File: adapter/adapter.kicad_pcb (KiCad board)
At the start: 2 copper layers, 93.5 x 50.8 mm, 42 parts, among them J1 Serial, J10 Ribbon, J11 Ribbon, J12 Ribbon, J2 Serial, J3 battery charge, J4 RGB, J5 RGB, J6 battery charge, J7 trackball, J8 trackball, J9 Ribbon, SW1 SW_SPST, SW2 SW_SPST, SW3 SW_SPDT, SW4 SW_SPDT, U1 eliteC, U2 eliteC

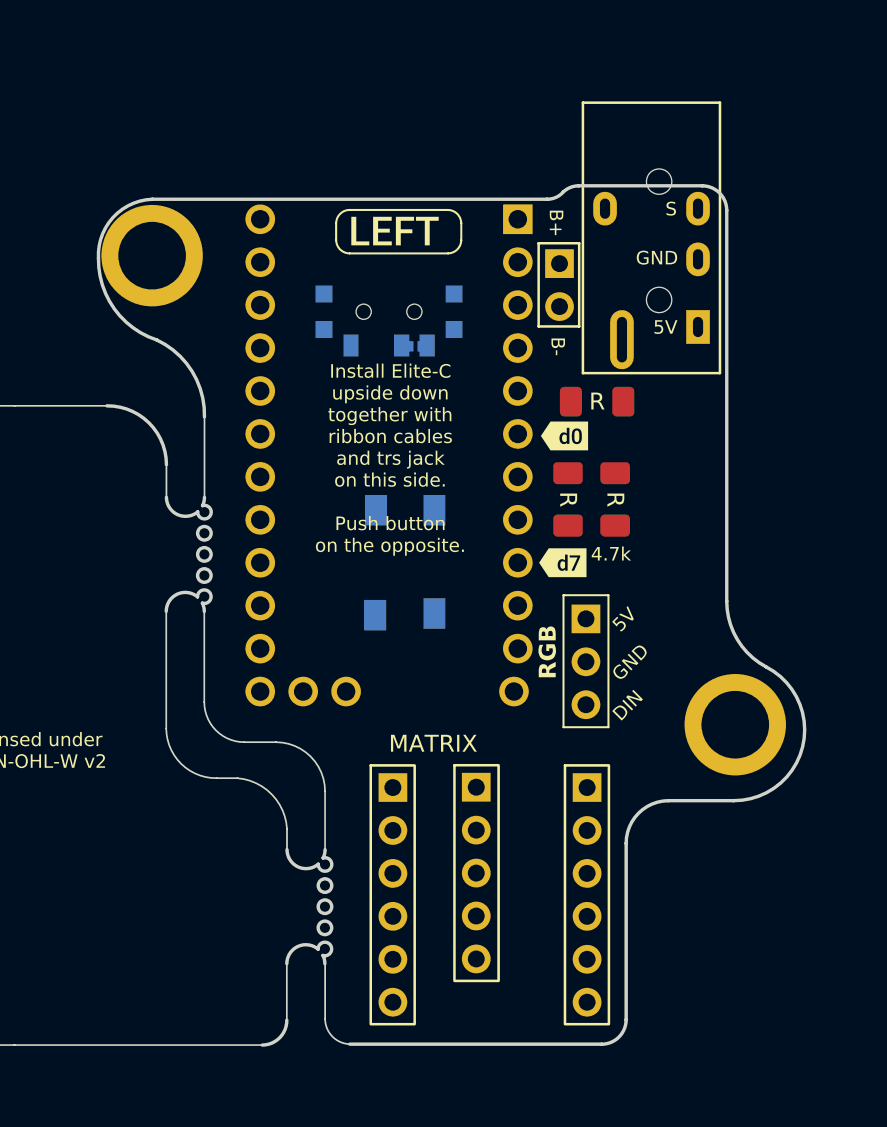
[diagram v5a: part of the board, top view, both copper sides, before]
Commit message: pcb: remove all footprints for rhs
Signed-off-by: Anant Thazhemadam <anant.thazhemadam@gmail.com>
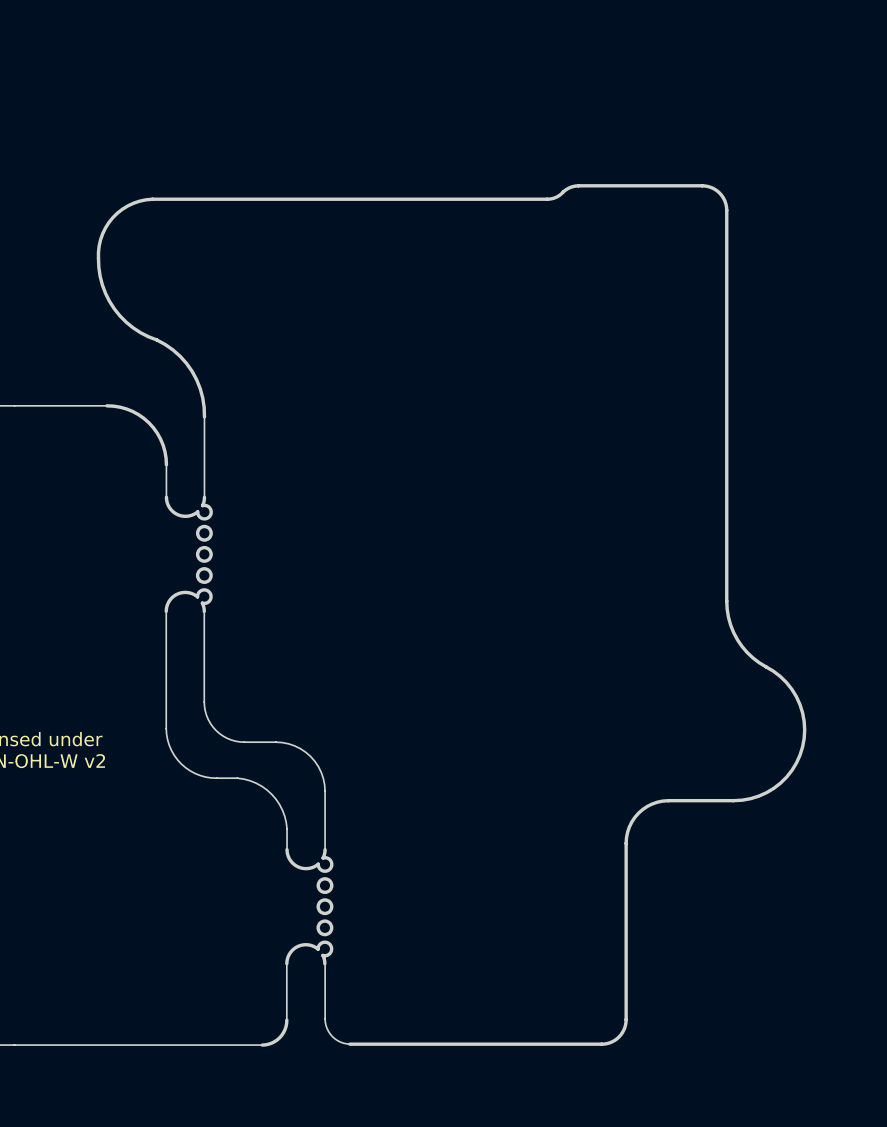
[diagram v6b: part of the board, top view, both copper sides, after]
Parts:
- removed H1, H3: M4, library:MountingHole_4mm_Pad_thin
- removed J11: Ribbon, library:5_PinHeader
- removed J12: Ribbon, library:6_PinHeader
- removed J2: Serial, library:Jack_3.5mm_PJ320E_Horizontal
- removed J5: RGB, library:header1x03
- removed J6: battery charge, library:PinHeader_1x02_P2.54mm_Vertical
- removed J8: trackball, library:6_PinHeader
- removed JP2: Jumper_2_Open, library:power_switch_jumper
- removed R1, R3, R5: 5.1k, library:R_1206_handsolder
- removed SW2: SW_SPST, library:PushSwitch
- removed SW4: SW_SPDT, library:SW_SPDT+H-MSK12C01_hor(7pin_SMD)
- removed U2: eliteC, library:Elite-C
- removed the kibuzzard-61F01C84 at (174.5, 89.2)
- removed kibuzzard-6208EE22: G***, kibuzzard-6208EE22
- removed kibuzzard-6208EFFE (x2): G***, kibuzzard-6208EFFE
- removed kibuzzard-62094D1C: G***, kibuzzard-62094D1C
- removed the kibuzzard-620B8593 at (177.5, 78.6)

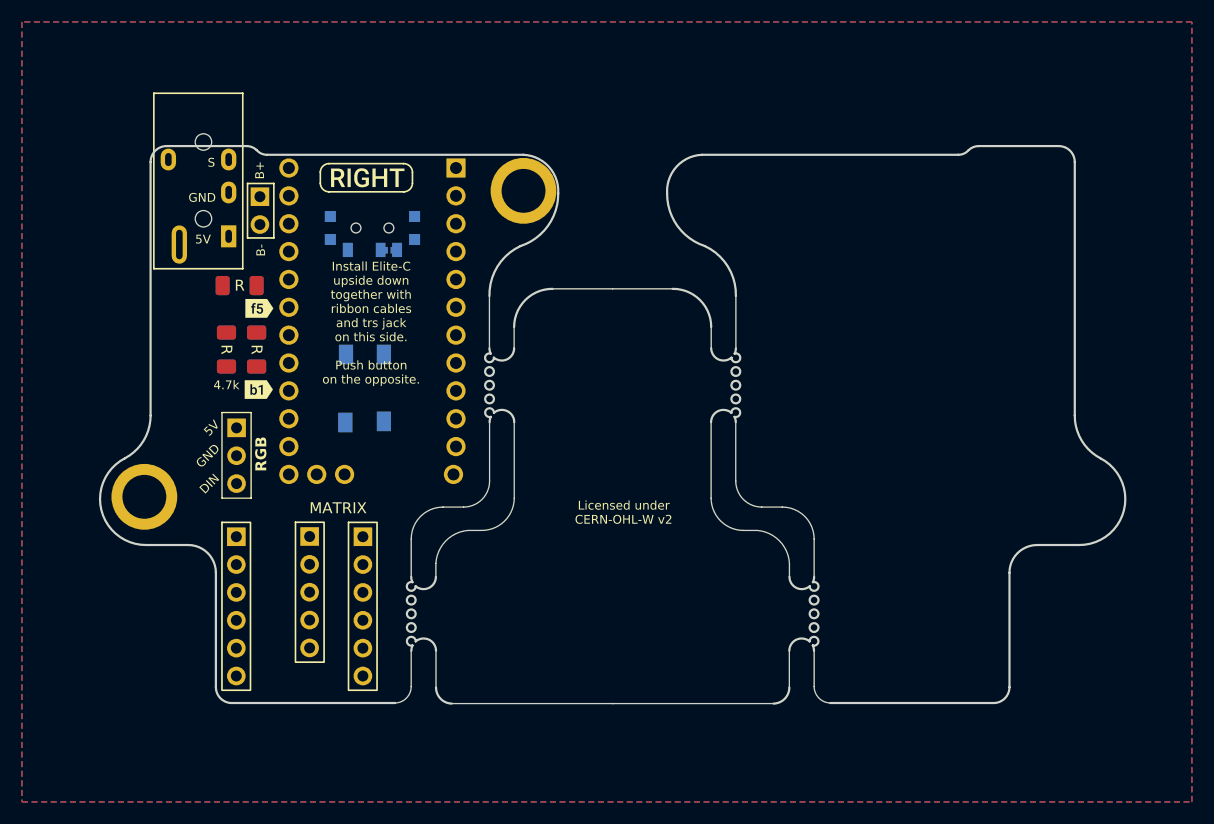
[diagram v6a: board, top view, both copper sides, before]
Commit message: pcb: fix outline drc errors
Signed-off-by: Anant Thazhemadam <anant.thazhemadam@gmail.com>
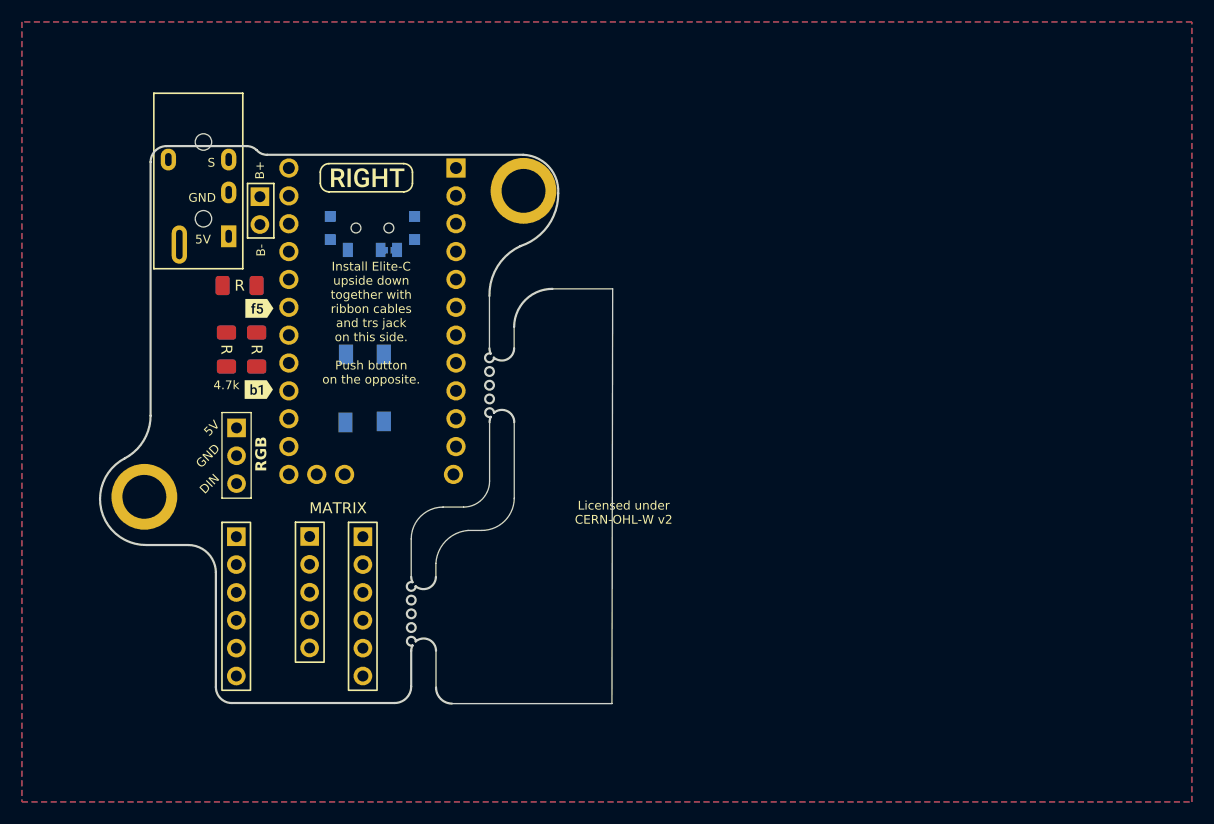
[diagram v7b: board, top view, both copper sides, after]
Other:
- board size 93.5 x 50.8 mm -> 46.7 x 50.8 mm

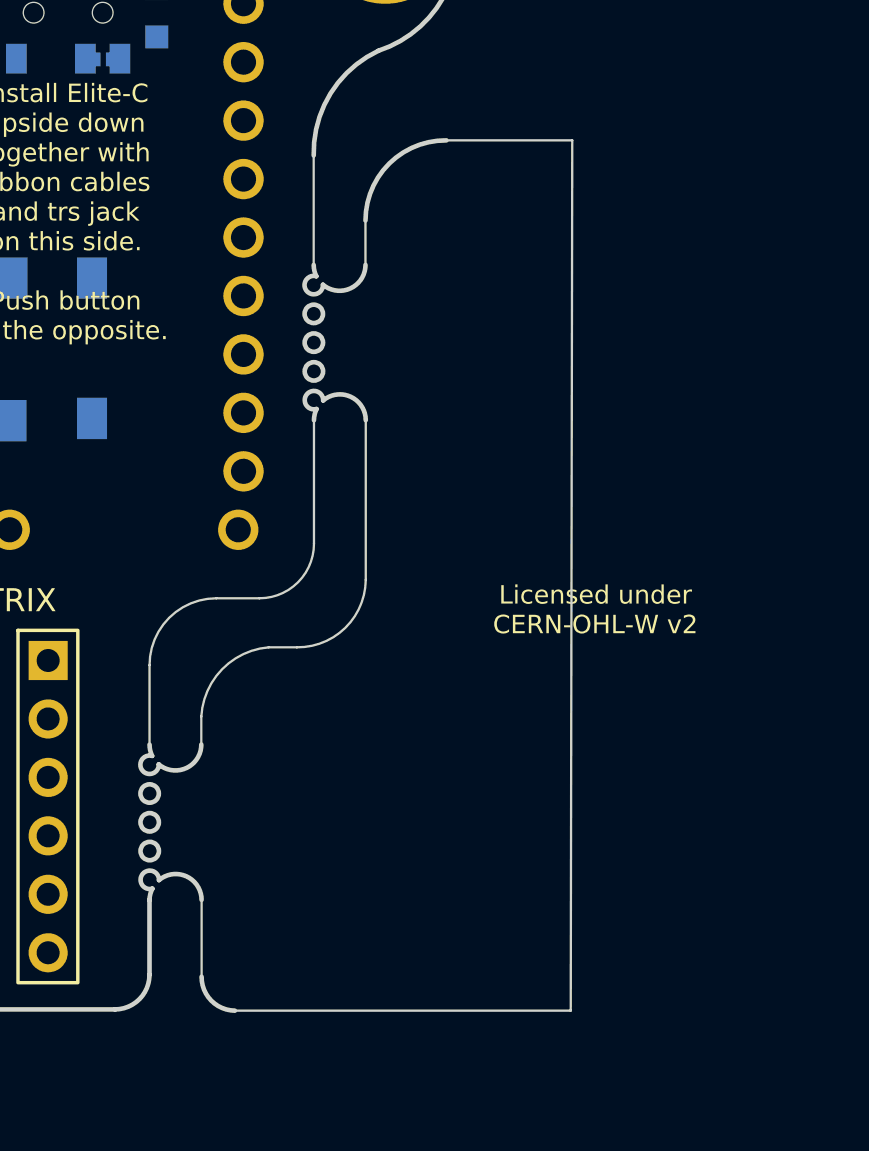
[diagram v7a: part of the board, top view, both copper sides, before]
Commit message: pcb: remove middle breakoff partition
Signed-off-by: Anant Thazhemadam <anant.thazhemadam@gmail.com>
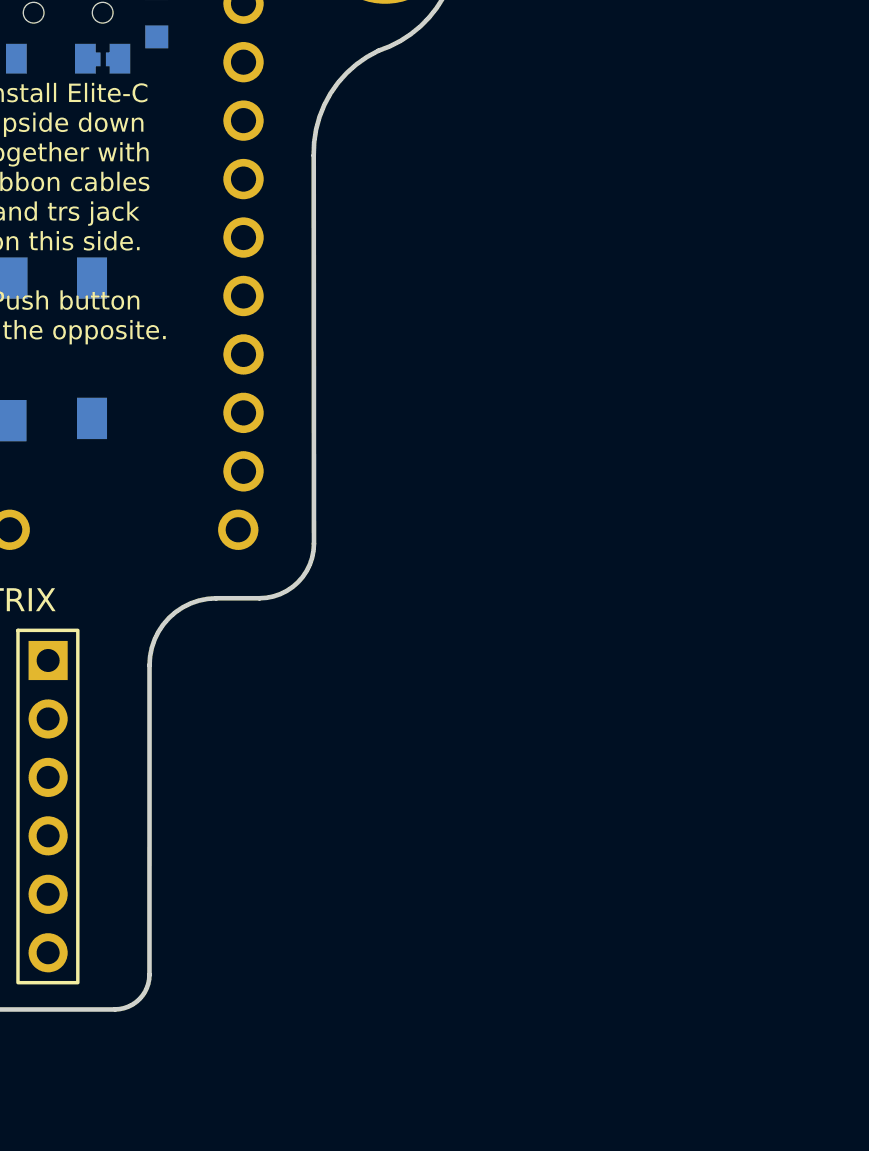
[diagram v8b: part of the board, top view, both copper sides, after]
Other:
- board size 46.7 x 50.8 mm -> 41.8 x 50.8 mm
- board text removed: "Licensed under CERN-OHL-W v2"
